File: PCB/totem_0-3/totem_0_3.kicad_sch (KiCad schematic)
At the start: 126 parts, among them J1 MJ-4PP-9, J2 MJ-4PP-9, U1 xiao-ble, U2 xiao-ble

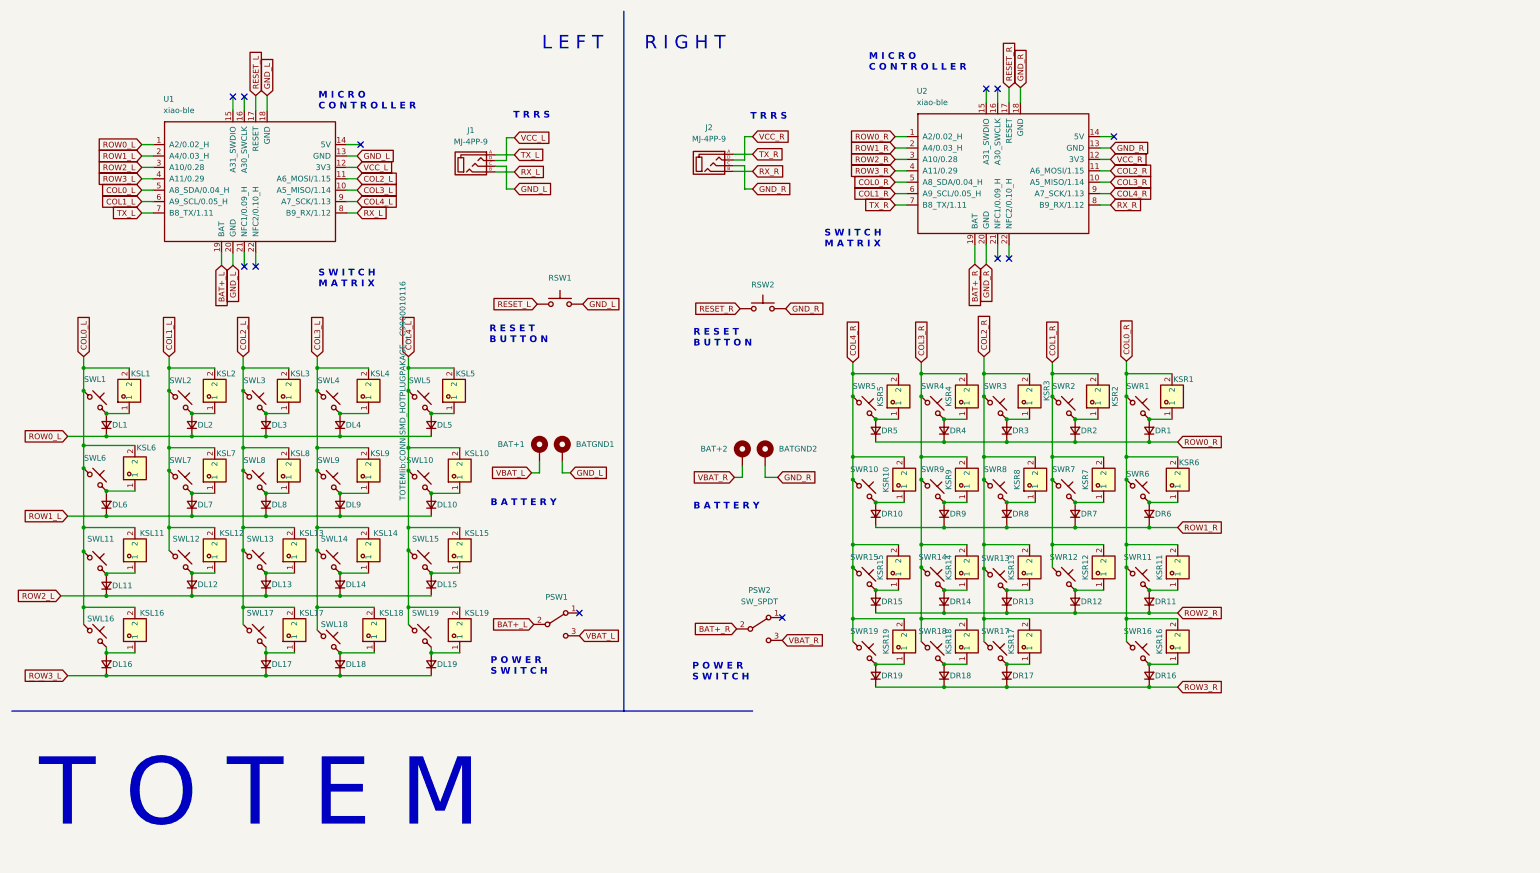
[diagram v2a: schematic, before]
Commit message: adding leds to left, wip
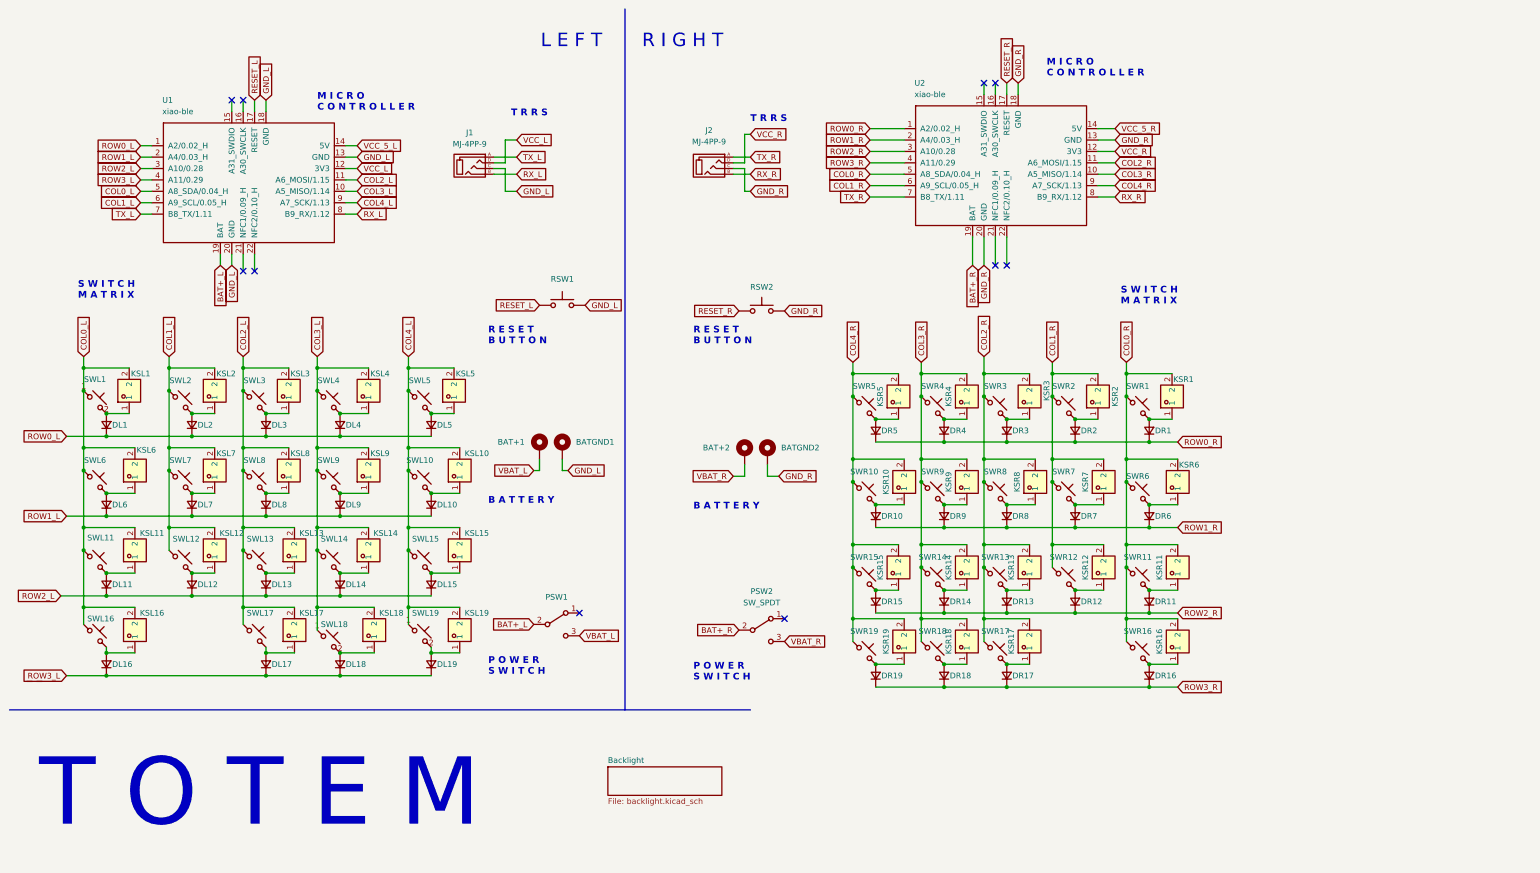
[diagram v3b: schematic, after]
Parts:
- BAT+1, BAT+2, BATGND1, BATGND2, SWL1, SWL10, SWL11, SWL12, SWL13, SWL14, SWL15, SWL16, SWL17, SWL18, SWL19, SWL2, SWL3, SWL4, SWL5, SWL6, SWL7, SWL8, SWL9, SWR1, SWR10, SWR11, SWR12, SWR13, SWR14, SWR15, SWR16, SWR17, SWR18, SWR19, SWR2, SWR3, SWR4, SWR5, SWR6, SWR7, SWR8, SWR9, U1, U2: now in the parts list
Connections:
- net VCC_5_L: now reaches U1.14 (5V)
- net VCC_5_R: now reaches U2.14 (5V)
- no-connect marks 12 -> 10
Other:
- added sheet Backlight (backlight.kicad_sch)
- moved on the sheet: BAT+1, BAT+2, BATGND1, BATGND2, DR10, DR6, DR7, DR8, DR9, J1, J2, KSL6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

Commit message: updating kicad footprint and shematics
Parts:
- removed J1, J2: MJ-4PP-9, TOTEMlib:MJ-4PP-9_1side, symbol kbd:MJ-4PP-9
- removed RSW1, RSW2: SW_Push, TOTEMlib:SKHLLCA010, symbol Switch:SW_Push
- added J1, J2: PJ-320A, TOTEMlib:AUDIO-TH_XKB_PJ-320A, symbol Totem_lib:PJ-320A
- added RSW1, RSW2: SKHLLCA010, TOTEMlib:KEY-TH_SKHLLCA010, symbol Totem_lib:SKHLLCA010
- BAT+1, BAT+2, BATGND1, BATGND2, KSL1, KSL10, KSL11, KSL12, KSL13, KSL14, KSL15, KSL16, KSL17, KSL18, KSL19, KSL2, KSL3, KSL4, KSL5, KSL6, KSL7, KSL8, KSL9, KSR1, KSR10, KSR11, KSR12, KSR13, KSR14, KSR15, KSR16, KSR17, KSR18, KSR19, KSR2, KSR3, KSR4, KSR5, KSR6, KSR7, KSR8, KSR9, PSW1, PSW2, SWL1, SWL10, SWL11, SWL12, SWL13, SWL14, SWL15, SWL16, SWL17, SWL18, SWL19, SWL2, SWL3, SWL4, SWL5, SWL6, SWL7, SWL8, SWL9, SWR1, SWR10, SWR11, SWR12, SWR13, SWR14, SWR15, SWR16, SWR17, SWR18, SWR19, SWR2, SWR3, SWR4, SWR5, SWR6, SWR7, SWR8, SWR9, U1, U2: now left out of the parts list
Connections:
- net GND_L: now also J1.3, RSW1.2
- net GND_R: now also J2.3, RSW2.2
- net RESET_L: now also RSW1.1
- net RESET_R: now also RSW2.1
- net RX_L: now also J1.2
- net RX_R: now also J2.2
- net TX_L: now also J1.5
- net TX_R: now also J2.5
- net VCC_L: now also J1.4
- net VCC_R: now also J2.4
- no-connect marks 10 -> 12
